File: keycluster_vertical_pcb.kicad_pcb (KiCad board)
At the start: 2 copper layers, 18.4 x 4.8 mm, 2 parts

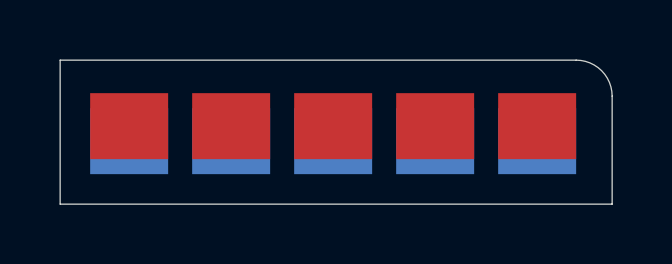
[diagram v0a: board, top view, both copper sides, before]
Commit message: Vertical pcb.
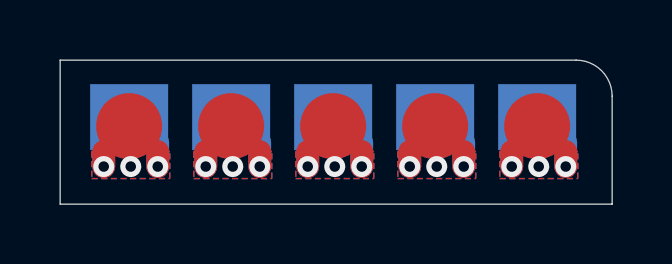
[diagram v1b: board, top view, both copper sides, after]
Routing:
- net (no net): track 0.00 -> 13.0 mm, vias 0 -> 15
- added copper zone on B.Cu, net (none)
- added copper zone on F.Cu, net (none)
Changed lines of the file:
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@@
     (thickness 1.6)
     (drawings 10)
-    (tracks 0)
+    (tracks 35)
     (zones 0)
     (modules 2)
@@
       (effects (font (size 1.27 1.27) (thickness 0.15)) (justify mirror))
     )
-    (pad 2 smd rect (at -0.1 10.1 270) (size 2.2 2.6) (layers F.Cu F.Mask))
-    (pad 3 smd rect (at -0.1 6.7 270) (size 2.2 2.6) (layers F.Cu F.Mask))
-    (pad 5 smd rect (at -0.1 -0.1 270) (size 2.2 2.6) (layers F.Cu F.Mask))
-    (pad 4 smd rect (at -0.1 3.3 270) (size 2.2 2.6) (layers F.Cu F.SilkS))
-    (pad 1 smd rect (at -0.1 13.5 270) (size 2.2 2.6) (layers F.Cu F.Mask))
+    (pad 2 smd circle (at -0.1 10.1 270) (size 2.2 2.2) (layers F.Cu F.Mask))
+    (pad 3 smd circle (at -0.1 6.7 270) (size 2.2 2.2) (layers F.Cu F.Mask))
+    (pad 5 smd circle (at -0.1 -0.1 270) (size 2.2 2.2) (layers F.Cu F.Mask))
+    (pad 4 smd circle (at -0.1 3.3 270) (size 2.2 2.2) (layers F.Cu F.Mask))
+    (pad 1 smd circle (at -0.1 13.5 270) (size 2.2 2.2) (layers F.Cu F.Mask))
   )
   (module "" (layer F.Cu)
@@
       (effects (font (size 1.27 1.27) (thickness 0.15)))
     )
-    (pad 2 smd rect (at -0.1 -10.1 90) (size 2.2 2.6) (layers B.Cu B.Mask))
-    (pad 3 smd rect (at -0.1 -6.7 90) (size 2.2 2.6) (layers B.Cu B.Mask))
-    (pad 5 smd rect (at -0.1 0.1 90) (size 2.2 2.6) (layers B.Cu B.Mask))
-    (pad 4 smd rect (at -0.1 -3.3 90) (size 2.2 2.6) (layers B.Cu B.SilkS))
-    (pad 1 smd rect (at -0.1 -13.5 90) (size 2.2 2.6) (layers B.Cu B.Mask))
+    (pad 2 smd rect (at 0.700006 -10.1 90) (size 2.2 2.6) (layers B.Cu B.Mask))
+    (pad 3 smd rect (at 0.700006 -6.7 90) (size 2.2 2.6) (layers B.Cu B.Mask))
+    (pad 5 smd rect (at 0.700006 0.1 90) (size 2.2 2.6) (layers B.Cu B.Mask))
+    (pad 4 smd rect (at 0.700006 -3.3 90) (size 2.2 2.6) (layers B.Cu B.Mask))
+    (pad 1 smd rect (at 0.700006 -13.5 90) (size 2.2 2.6) (layers B.Cu B.Mask))
   )
   (gr_line (start 218.399994 150) (end 200 150) (angle 90) (layer Edge.Cuts) (width 0.01))
@@
   (gr_circle (center 205.699997 147.400009) (end 206.599997 147.400009) (layer Eco1.User) (width 0.01))
   (gr_circle (center 215.899994 147.400009) (end 216.799994 147.400009) (layer Eco1.User) (width 0.01))
+  (via (at 201.453003 148.747006) (size 0.7) (drill 0.35) (layers F.Cu B.Cu) (net 0))
+  (via (at 203.253003 148.747006) (size 0.7) (drill 0.35) (layers F.Cu B.Cu) (net 0))
+  (via (at 202.353003 148.747006) (size 0.7) (drill 0.35) (layers F.Cu B.Cu) (net 0))
+  (segment (start 203.253003 147.947006) (end 203.253003 148.747006) (width 0.762) (layer B.Cu) (net 0))
+  (segment (start 203.253003 148.747006) (end 203.253003 148.247006) (width 0.762) (layer F.Cu) (net 0))
+  (segment (start 201.453003 147.947006) (end 201.453003 148.747006) (width 0.762) (layer B.Cu) (net 0))
+  (segment (start 201.453003 148.747006) (end 201.453003 148.247006) (width 0.762) (layer F.Cu) (net 0))
+  (via (at 204.853003 148.747006) (size 0.7) (drill 0.35) (layers F.Cu B.Cu) (net 0))
+  (via (at 206.653003 148.747006) (size 0.7) (drill 0.35) (layers F.Cu B.Cu) (net 0))
+  (via (at 205.753003 148.747006) (size 0.7) (drill 0.35) (layers F.Cu B.Cu) (net 0))
+  (segment (start 206.653003 147.947006) (end 206.653003 148.747006) (width 0.762) (layer B.Cu) (net 0))
+  (segment (start 206.653003 148.747006) (end 206.653003 148.247006) (width 0.762) (layer F.Cu) (net 0))
+  (segment (start 204.853003 147.947006) (end 204.853003 148.747006) (width 0.762) (layer B.Cu) (net 0))
+  (segment (start 204.853003 148.747006) (end 204.853003 148.247006) (width 0.762) (layer F.Cu) (net 0))
+  (via (at 215.053003 148.747006) (size 0.7) (drill 0.35) (layers F.Cu B.Cu) (net 0))
+  (via (at 216.853003 148.747006) (size 0.7) (drill 0.35) (layers F.Cu B.Cu) (net 0))
+  (via (at 215.953003 148.747006) (size 0.7) (drill 0.35) (layers F.Cu B.Cu) (net 0))
+  (segment (start 216.853003 147.947006) (end 216.853003 148.747006) (width 0.762) (layer B.Cu) (net 0))
+  (segment (start 216.853003 148.747006) (end 216.853003 148.247006) (width 0.762) (layer F.Cu) (net 0))
+  (segment (start 215.053003 147.947006) (end 215.053003 148.747006) (width 0.762) (layer B.Cu) (net 0))
+  (segment (start 215.053003 148.747006) (end 215.053003 148.247006) (width 0.762) (layer F.Cu) (net 0))
+  (via (at 211.653 148.747) (size 0.7) (drill 0.35) (layers F.Cu B.Cu) (net 0))
+  (via (at 213.453 148.747) (size 0.7) (drill 0.35) (layers F.Cu B.Cu) (net 0))
+  (via (at 212.553 148.747) (size 0.7) (drill 0.35) (layers F.Cu B.Cu) (net 0))
+  (segment (start 213.453 147.947) (end 213.453 148.747) (width 0.762) (layer B.Cu) (net 0))
+  (segment (start 213.453 148.747) (end 213.453 148.247) (width 0.762) (layer F.Cu) (net 0))
+  (segment (start 211.653 147.947) (end 211.653 148.747) (width 0.762) (layer B.Cu) (net 0))
+  (segment (start 211.653 148.747) (end 211.653 148.247) (width 0.762) (layer F.Cu) (net 0))
+  (via (at 208.253003 148.747006) (size 0.7) (drill 0.35) (layers F.Cu B.Cu) (net 0))
+  (via (at 210.053003 148.747006) (size 0.7) (drill 0.35) (layers F.Cu B.Cu) (net 0))
+  (via (at 209.153003 148.747006) (size 0.7) (drill 0.35) (layers F.Cu B.Cu) (net 0))
+  (segment (start 210.053003 147.947006) (end 210.053003 148.747006) (width 0.762) (layer B.Cu) (net 0))
+  (segment (start 210.053003 148.747006) (end 210.053003 148.247006) (width 0.762) (layer F.Cu) (net 0))
+  (segment (start 208.253003 147.947006) (end 208.253003 148.747006) (width 0.762) (layer B.Cu) (net 0))
+  (segment (start 208.253003 148.747006) (end 208.253003 148.247006) (width 0.762) (layer F.Cu) (net 0))
+  (zone (net 0) (net_name "") (layer F.Cu) (hatch edge 0.508)
+    (connect_pads (clearance 0))
+    (min_thickness 0.0254)
+    (fill yes (arc_segments 16) (thermal_gap 0) (thermal_bridge_width 0.0255))
+    (polygon
+      (pts
+        (xy 201.053003 148.247006) (xy 201.053003 149.147006) (xy 203.653003 149.147006) (xy 203.653003 148.247006)
+      )
+    )
+  )
+  (zone (net 0) (net_name "") (layer B.Cu) (hatch edge 0.508)
+    (connect_pads (clearance 0))
+    (min_thickness 0.0254)
+    (fill yes (arc_segments 16) (thermal_gap 0) (thermal_bridge_width 0.0255))
+    (polygon
+      (pts
+        (xy 201.053003 148.247006) (xy 201.053003 149.147006) (xy 203.653003 149.147006) (xy 203.653003 148.247006)
+      )
+    )
+  )
+  (zone (net 0) (net_name "") (layer F.Cu) (hatch edge 0.508)
+    (connect_pads (clearance 0))
+    (min_thickness 0.0254)
+    (fill yes (arc_segments 16) (thermal_gap 0) (thermal_bridge_width 0.0255))
+    (polygon
+      (pts
+        (xy 204.453003 148.247006) (xy 204.453003 149.147006) (xy 207.053003 149.147006) (xy 207.053003 148.247006)
+      )
+    )
+  )
+  (zone (net 0) (net_name "") (layer B.Cu) (hatch edge 0.508)
+    (connect_pads (clearance 0))
+    (min_thickness 0.0254)
+    (fill yes (arc_segments 16) (thermal_gap 0) (thermal_bridge_width 0.0255))
+    (polygon
+      (pts
+        (xy 204.453003 148.247006) (xy 204.453003 149.147006) (xy 207.053003 149.147006) (xy 207.053003 148.247006)
+      )
+    )
+  )
+  (zone (net 0) (net_name "") (layer F.Cu) (hatch edge 0.508)
+    (connect_pads (clearance 0))
+    (min_thickness 0.0254)
+    (fill yes (arc_segments 16) (thermal_gap 0) (thermal_bridge_width 0.0255))
+    (polygon
+      (pts
+        (xy 214.653003 148.247006) (xy 214.653003 149.147006) (xy 217.253003 149.147006) (xy 217.253003 148.247006)
+      )
+    )
+  )
+  (zone (net 0) (net_name "") (layer B.Cu) (hatch edge 0.508)
+    (connect_pads (clearance 0))
+    (min_thickness 0.0254)
+    (fill yes (arc_segments 16) (thermal_gap 0) (thermal_bridge_width 0.0255))
+    (polygon
+      (pts
+        (xy 214.653003 148.247006) (xy 214.653003 149.147006) (xy 217.253003 149.147006) (xy 217.253003 148.247006)
+      )
+    )
+  )
+  (zone (net 0) (net_name "") (layer F.Cu) (hatch edge 0.508)
+    (connect_pads (clearance 0))
+    (min_thickness 0.0254)
+    (fill yes (arc_segments 16) (thermal_gap 0) (thermal_bridge_width 0.0255))
+    (polygon
+      (pts
+        (xy 211.253 148.247) (xy 211.253 149.147) (xy 213.853 149.147) (xy 213.853 148.247)
+      )
+    )
+  )
+  (zone (net 0) (net_name "") (layer B.Cu) (hatch edge 0.508)
+    (connect_pads (clearance 0))
+    (min_thickness 0.0254)
+    (fill yes (arc_segments 16) (thermal_gap 0) (thermal_bridge_width 0.0255))
+    (polygon
+      (pts
+        (xy 211.253 148.247) (xy 211.253 149.147) (xy 213.853 149.147) (xy 213.853 148.247)
+      )
+    )
+  )
+  (zone (net 0) (net_name "") (layer F.Cu) (hatch edge 0.508)
+    (connect_pads (clearance 0))
+    (min_thickness 0.0254)
+    (fill yes (arc_segments 16) (thermal_gap 0) (thermal_bridge_width 0.0255))
+    (polygon
+      (pts
+        (xy 207.853003 148.247006) (xy 207.853003 149.147006) (xy 210.453003 149.147006) (xy 210.453003 148.247006)
+      )
+    )
+  )
+  (zone (net 0) (net_name "") (layer B.Cu) (hatch edge 0.508)
+    (connect_pads (clearance 0))
+    (min_thickness 0.0254)
+    (fill yes (arc_segments 16) (thermal_gap 0) (thermal_bridge_width 0.0255))
+    (polygon
+      (pts
+        (xy 207.853003 148.247006) (xy 207.853003 149.147006) (xy 210.453003 149.147006) (xy 210.453003 148.247006)
+      )
+    )
+  )
 )
